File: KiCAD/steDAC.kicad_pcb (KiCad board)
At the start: 2 copper layers, 100 x 80 mm, 154 parts, among them IC10 ADP7182ACPZN-R7, IC11 ADP150AUJZ-3.3-R7, IC2 ES9038Q2M, IC3 ATSAMS70N20A-AN, IC4 ADP150AUJZ-3.3-R7, IC5 ADP150AUJZ-3.3-R7, IC6 ADP150AUJZ-3.3-R7, IC7 ADP150AUJZ-3.3-R7, IC8 LT1026CS8#PBF, IC9 ADP7118ARDZ, J2 USB4105-GF-A, J3 Conn_02x05_Odd_Even, J5 Conn_01x02, J6 Conn_01x04, J7 STX-3120-5B-284C, U2 OPA1612-Q1, U3 OPA1612-Q1, U4 OPA1622, Y2 SiT8209AI-21-33S-100.000000X, Y3 12MHz

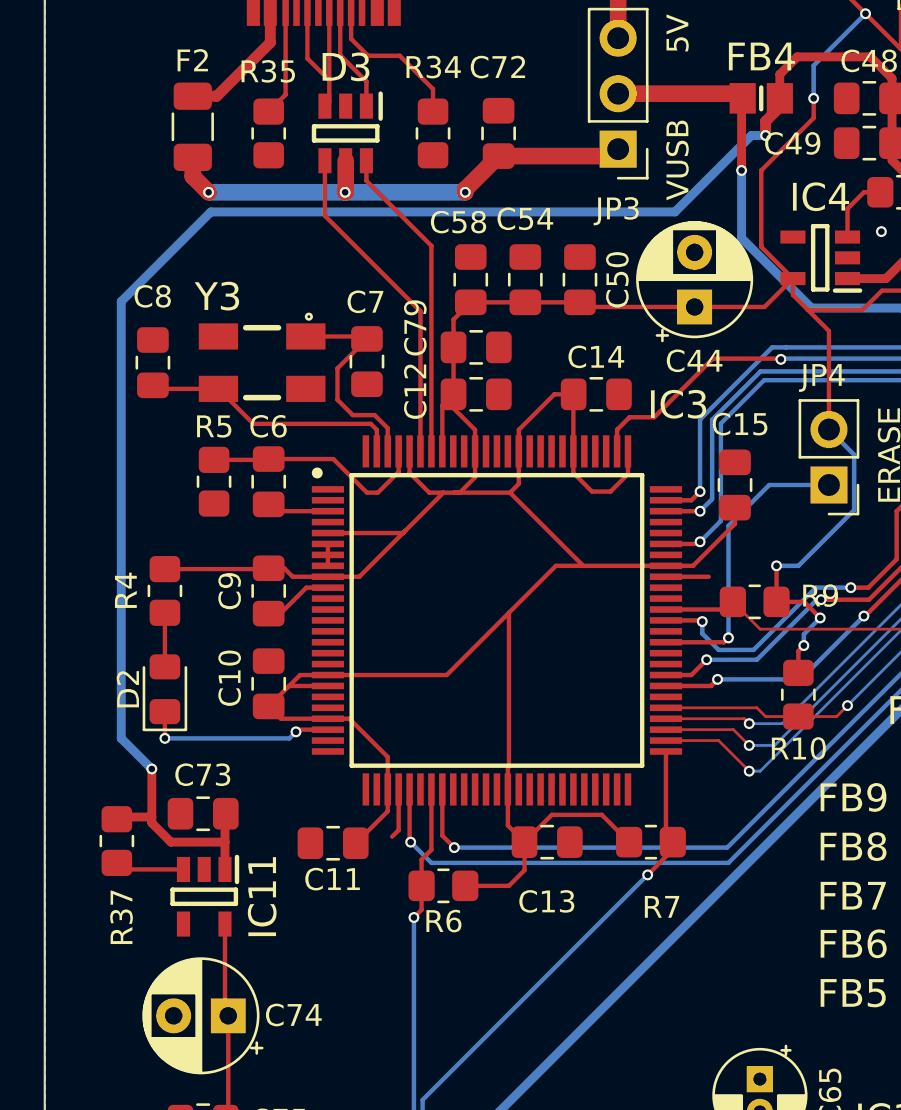
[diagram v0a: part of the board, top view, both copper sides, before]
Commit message: Updating BOM generator script
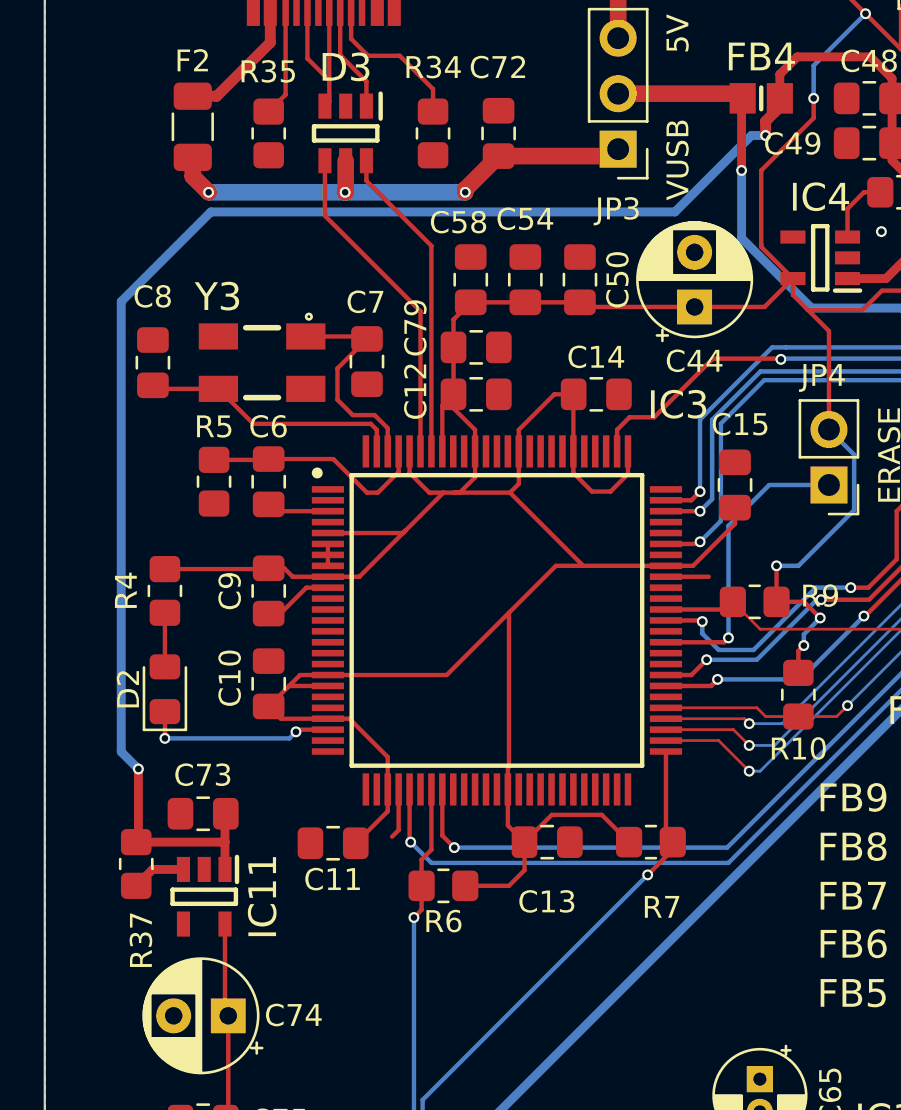
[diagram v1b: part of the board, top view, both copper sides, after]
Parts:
- moved R37 1.37 mm to (92.1, 100.9)
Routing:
- net Net-(IC11-Pad3): track 3.17 -> 2.47 mm
- net MCU_5V: track 86.2 -> 85.6 mm
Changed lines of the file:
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@@
       (sketchpadsonfab false)
       (subtractmaskfromsilk false)
-      (outputformat 4)
+      (outputformat 1)
       (mirror false)
       (drillshape 0)
@@
   )
   (footprint "Resistor_SMD:R_0805_2012Metric_Pad1.20x1.40mm_HandSolder" (layer "F.Cu")
-    (at 91.2125 99.85 90)
+    (at 92.1 100.9 90)
     (descr "Resistor SMD 0805 (2012 Metric), square (rectangular) end terminal, IPC_7351 nominal with elongated pad for handsoldering. (Body size source: IPC-SM-782 page 72, https://www.pcb-3d.com/wordpress/wp-content/uploads/ipc-sm-782a_amendment_1_and_2.pdf), generated with kicad-footprint-generator")
     (tags "resistor handsolder")
@@
   )
   (dimension (type aligned) (layer "Cmts.User")
+    (pts (xy 156.1625 131.65) (xy 187.9 131.65))
+    (height 12.749999)
+    (gr_text "31.7375 mm" (at 172.03125 143.249999) (layer "Cmts.User")
+      (effects (font (size 1 1) (thickness 0.15)))
+    )
+    (format (units 3) (units_format 1) (precision 4))
+    (style (thickness 0.15) (arrow_length 1.27) (text_position_mode 0) (extension_height 0.58642) (extension_offset 0.5) keep_text_aligned)
+  )
+  (dimension (type aligned) (layer "Cmts.User")
     (pts (xy 156.1625 131.65) (xy 156.1625 134.65))
     (height 15.75)
@@
     (style (thickness 0.15) (arrow_length 1.27) (text_position_mode 0) (extension_height 0.58642) (extension_offset 0.5) keep_text_aligned)
   )
+  (dimension (type aligned) (layer "Cmts.User")
+    (pts (xy 96.2175 60.415) (xy 87.9 60.415))
+    (height 11.605391)
+    (gr_text "8.3175 mm" (at 92.05875 47.659609) (layer "Cmts.User")
+      (effects (font (size 1 1) (thickness 0.15)))
+    )
+    (format (units 3) (units_format 1) (precision 4))
+    (style (thickness 0.15) (arrow_length 1.27) (text_position_mode 0) (extension_height 0.58642) (extension_offset 0.5) keep_text_aligned)
+  )
   (segment (start 160.7125 92.15) (end 160.7125 91.6375) (width 0.2) (layer "F.Cu") (net 1))
   (segment (start 160.7125 91.6375) (end 162.9125 89.4375) (width 0.2) (layer "F.Cu") (net 1))
@@
   (segment (start 170.375 128.65) (end 167.6125 128.65) (width 0.2032) (layer "F.Cu") (net 26))
   (segment (start 126.7 68.6875) (end 128.1625 70.15) (width 0.4064) (layer "F.Cu") (net 27))
-  (segment (start 92.8125 98.75) (end 91.3125 98.75) (width 0.4064) (layer "F.Cu") (net 27))
   (segment (start 96.2 98.6) (end 96.1625 98.6375) (width 0.2032) (layer "F.Cu") (net 27))
-  (segment (start 92.8125 99.023085) (end 93.689415 99.9) (width 0.4064) (layer "F.Cu") (net 27))
   (segment (start 121.5625 66.25) (end 120.9125 66.9) (width 0.5) (layer "F.Cu") (net 27))
-  (segment (start 93.689415 99.9) (end 96.1625 99.9) (width 0.4064) (layer "F.Cu") (net 27))
   (segment (start 122.3625 63.95) (end 125.7125 63.95) (width 0.4064) (layer "F.Cu") (net 27))
   (segment (start 121.5625 64.75) (end 122.3625 63.95) (width 0.4064) (layer "F.Cu") (net 27))
-  (segment (start 91.3125 98.75) (end 91.2125 98.85) (width 0.4064) (layer "F.Cu") (net 27))
   (segment (start 126.425 74.1) (end 124.6625 74.1) (width 0.4064) (layer "F.Cu") (net 27))
-  (segment (start 92.8125 98.75) (end 92.8125 99.023085) (width 0.4064) (layer "F.Cu") (net 27))
+  (segment (start 96.1625 99.9) (end 92.1 99.9) (width 0.4064) (layer "F.Cu") (net 27))
   (segment (start 127.775 72.75) (end 126.425 74.1) (width 0.4064) (layer "F.Cu") (net 27))
   (segment (start 126.7 64.9375) (end 126.7 65.85) (width 0.4064) (layer "F.Cu") (net 27))
   (segment (start 126.7 67.9) (end 126.7 68.6875) (width 0.4064) (layer "F.Cu") (net 27))
   (segment (start 125.7125 63.95) (end 126.7 64.9375) (width 0.4064) (layer "F.Cu") (net 27))
-  (segment (start 92.8125 96.55) (end 92.8125 98.75) (width 0.4064) (layer "F.Cu") (net 27))
   (segment (start 121.5625 65.85) (end 121.5625 64.75) (width 0.4064) (layer "F.Cu") (net 27))
   (segment (start 128.1625 70.15) (end 128.1625 72.3625) (width 0.4064) (layer "F.Cu") (net 27))
   (segment (start 120.9125 66.9) (end 120.9125 67.55) (width 0.5) (layer "F.Cu") (net 27))
+  (segment (start 92.1 99.9) (end 92.2 99.8) (width 0.4064) (layer "F.Cu") (net 27))
   (segment (start 126.7 65.85) (end 126.7 67.9) (width 0.4064) (layer "F.Cu") (net 27))
   (segment (start 128.1625 72.3625) (end 127.775 72.75) (width 0.4064) (layer "F.Cu") (net 27))
   (segment (start 96.1625 98.6375) (end 96.1625 99.9) (width 0.4064) (layer "F.Cu") (net 27))
   (segment (start 121.5625 65.85) (end 121.5625 66.25) (width 0.2032) (layer "F.Cu") (net 27))
+  (segment (start 92.2 99.8) (end 92.2 96.55) (width 0.4064) (layer "F.Cu") (net 27))
   (segment (start 96.1625 99.9) (end 96.1625 101.15) (width 0.4064) (layer "F.Cu") (net 27))
-  (via (at 92.8125 96.55) (size 0.5) (drill 0.3) (layers "F.Cu" "B.Cu") (net 27))
+  (via (at 92.2 96.55) (size 0.5) (drill 0.3) (layers "F.Cu" "B.Cu") (net 27))
   (via (at 120.9125 67.55) (size 0.5) (drill 0.3) (layers "F.Cu" "B.Cu") (net 27))
-  (segment (start 120.2625 67.55) (end 116.7625 71.05) (width 0.4064) (layer "B.Cu") (net 27))
-  (segment (start 91.4125 95.15) (end 92.8125 96.55) (width 0.4064) (layer "B.Cu") (net 27))
-  (segment (start 116.7625 71.05) (end 95.5125 71.05) (width 0.4064) (layer "B.Cu") (net 27))
-  (segment (start 95.5125 71.05) (end 91.4125 75.15) (width 0.4064) (layer "B.Cu") (net 27))
-  (segment (start 120.9125 67.55) (end 120.2625 67.55) (width 0.4064) (layer "B.Cu") (net 27))
-  (segment (start 91.4125 75.15) (end 91.4125 95.15) (width 0.4064) (layer "B.Cu") (net 27))
+  (segment (start 95.5125 71.05) (end 116.7625 71.05) (width 0.4064) (layer "B.Cu") (net 27))
+  (segment (start 120.2625 67.55) (end 120.9125 67.55) (width 0.4064) (layer "B.Cu") (net 27))
+  (segment (start 116.7625 71.05) (end 120.2625 67.55) (width 0.4064) (layer "B.Cu") (net 27))
+  (segment (start 91.4125 75.15) (end 95.5125 71.05) (width 0.4064) (layer "B.Cu") (net 27))
+  (segment (start 92.2 96.55) (end 91.4125 95.7625) (width 0.4064) (layer "B.Cu") (net 27))
+  (segment (start 91.4125 95.7625) (end 91.4125 75.15) (width 0.4064) (layer "B.Cu") (net 27))
   (segment (start 141.875 85.65) (end 141.875 86.575) (width 0.4064) (layer "F.Cu") (net 28))
   (segment (start 114.9505 116.765) (end 112.5525 116.765) (width 0.4064) (layer "F.Cu") (net 28))
@@
   (segment (start 124.6625 70.9) (end 124.6625 72.2) (width 0.2032) (layer "F.Cu") (net 124))
   (segment (start 125.4125 70.15) (end 126.1625 70.15) (width 0.2032) (layer "F.Cu") (net 124))
-  (segment (start 91.2125 100.85) (end 91.5125 101.15) (width 0.2) (layer "F.Cu") (net 131))
-  (segment (start 91.5125 101.15) (end 94.2625 101.15) (width 0.2) (layer "F.Cu") (net 131))
+  (segment (start 92.85 101.15) (end 92.1 101.9) (width 0.4064) (layer "F.Cu") (net 131))
+  (segment (start 94.2625 101.15) (end 92.85 101.15) (width 0.4064) (layer "F.Cu") (net 131))
   (segment (start 105.6875 65.425) (end 105.6875 66.455) (width 0.2032) (layer "F.Cu") (net 134))
   (segment (start 104.1625 63.9) (end 105.6875 65.425) (width 0.2032) (layer "F.Cu") (net 134))

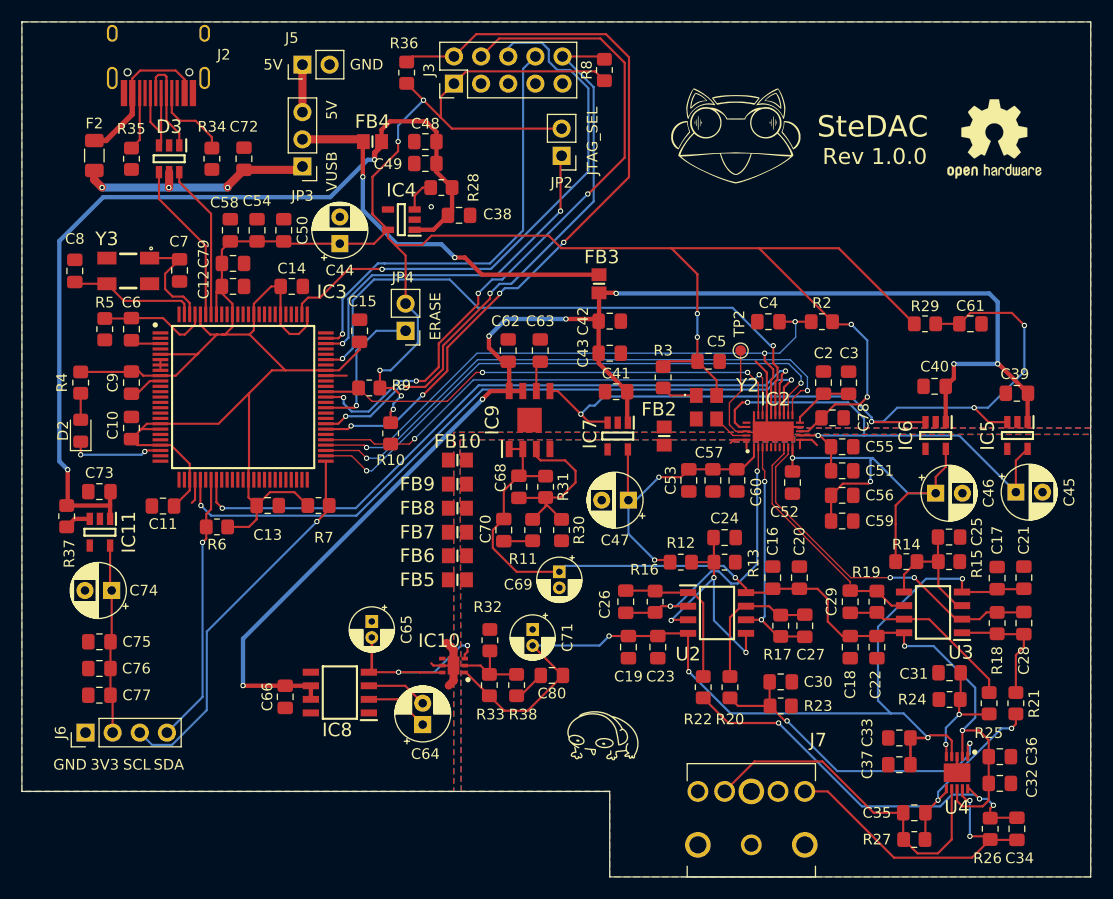
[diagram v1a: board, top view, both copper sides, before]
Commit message: [REV1.0.1] Rerouting some traces in the output stage. Adding rev1.0.1 gerbers
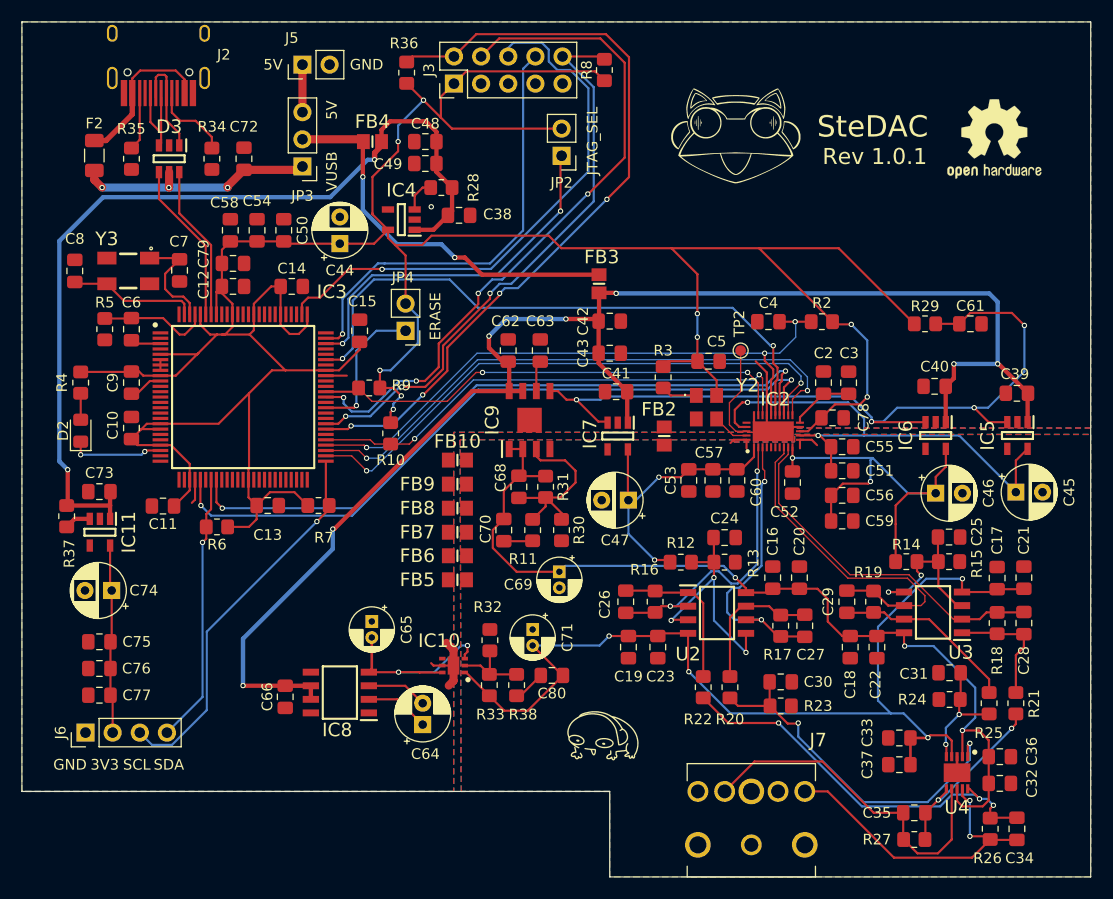
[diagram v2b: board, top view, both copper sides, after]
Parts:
- moved C29 0.31 mm to (165.1, 108.9)
- moved R19 0.31 mm to (167.6, 108.9)
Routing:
- net DAC_OUTL_P: track 22.5 -> 31.8 mm
- net DAC_OUTR_P: track 22.5 -> 27.0 mm
- net Net-(C30-Pad1): track 30.5 -> 34.1 mm
- net /Output Stage/VBias_L: track 13.0 -> 16.3 mm, vias 0 -> 2
- net DAC_5V: track 138.3 -> 139.4 mm
- net DAC_OUTL_N: track 33.7 -> 33.3 mm, vias 2 -> 0
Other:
- board text added: "Rev 1.0.1"
- board text removed: "Rev 1.0.0"

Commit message: Fixing 3.3V being fed to VDDCORE. Swaping 3.3V LDOs to onsemi ones with higher output current
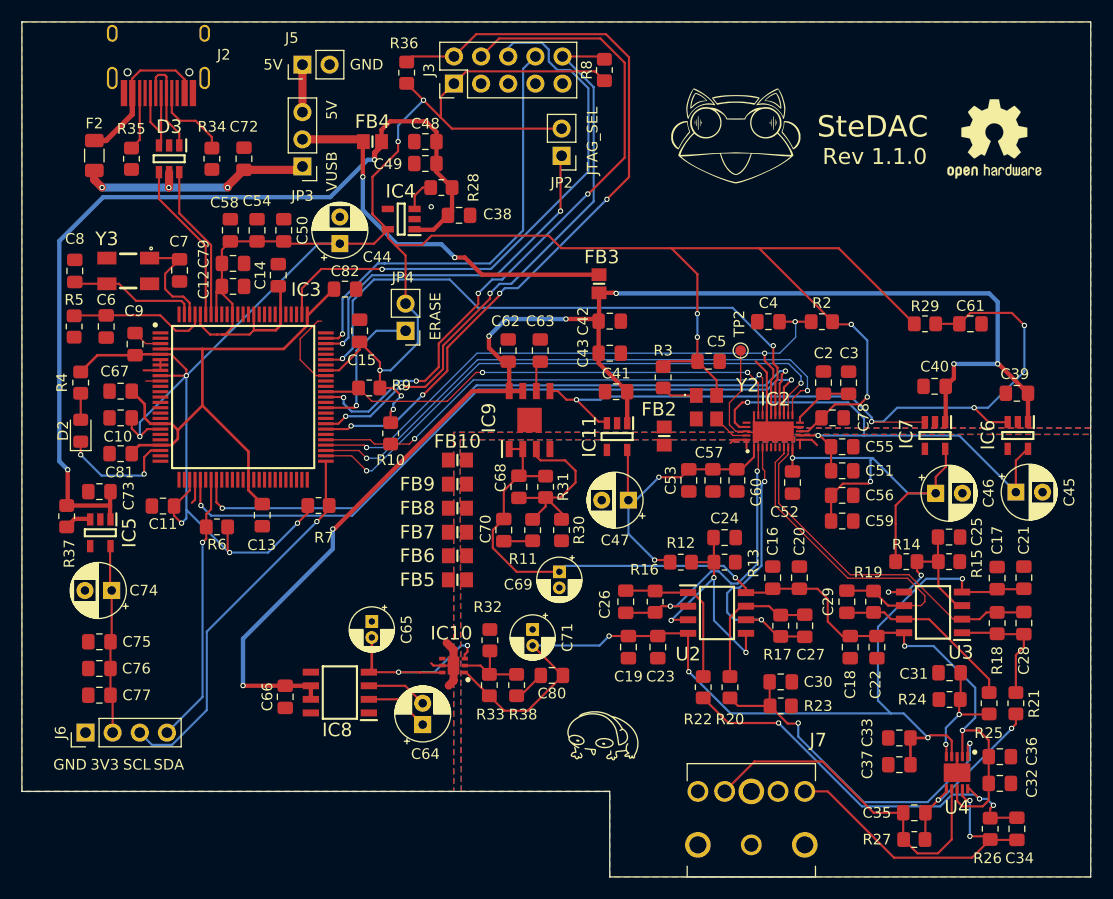
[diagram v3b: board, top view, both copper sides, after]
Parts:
- added C67: 0.1u, Capacitor_SMD:C_0805_2012Metric_Pad1.18x1.45mm_HandSolder, F.Cu at (97.2, 89.2)
- added C81: 0.1u, Capacitor_SMD:C_0805_2012Metric_Pad1.18x1.45mm_HandSolder, F.Cu at (97.2, 95.0)
- added C82: 0.1u, Capacitor_SMD:C_0805_2012Metric_Pad1.18x1.45mm_HandSolder, F.Cu at (118.2, 79.7)
- IC11, IC4, IC5, IC6, IC7: value ADP150AUJZ-3.3-R7 -> NCP161ASN330T1G; footprint SamacSys_Parts:SOT95P280X100-5N -> SamacSys_Parts:SOT95P280X145-5N
- U2, U3: value OPA1612-Q1 -> OPA1612
- moved IC5 86.3 mm to (95.2, 102.5)
- moved IC11 49.2 mm to (143.6, 93.5)
- moved IC7 29.7 mm to (173.3, 93.3)
- moved IC6 7.69 mm to (181.1, 93.3)
- moved C9 3.62 mm to (98.5, 84.8), turned to 90 degrees
- moved R5 2.87 mm to (92.8, 83.2)
- moved C6 2.38 mm to (95.8, 83.2)
- moved C14 1.64 mm to (111.9, 78.3), turned to 90 degrees
- moved C10 1.39 mm to (97.2, 91.7), turned to 180 degrees
- moved C13 1.04 mm to (110.4, 100.8), turned to -90 degrees
- moved IC4 0.05 mm to (123.4, 73.1)
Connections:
- C13 pad 1: +3V3 -> +1V2
- IC11 pad 1: MCU_5V -> DAC_5V
- IC11 pad 3: Net-(IC11-Pad3) -> DAC_PWR_EN
- IC11 pad 5: OLED_3V3 -> AVCC_R
- IC3 pad 18: +3V3 -> +1V2
- IC3 pad 22: +3V3 -> +1V2
- IC3 pad 39: +3V3 -> +1V2
- IC3 pad 4: unconnected-(IC3-Pad4) -> +1V2
- IC3 pad 76: +3V3 -> +1V2
- IC5 pad 1: DAC_5V -> MCU_5V
- IC5 pad 3: DAC_PWR_EN -> Net-(IC5-Pad3)
- IC5 pad 5: +3.3VDAC -> OLED_3V3
- IC6 pad 5: AVCC_L -> +3.3VDAC
- IC7 pad 5: AVCC_R -> AVCC_L
- R37 pad 1: Net-(IC11-Pad3) -> Net-(IC5-Pad3)
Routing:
- net +1V2: track 0.00 -> 51.6 mm
- net GND: track 30.7 -> 36.0 mm
- net Net-(C6-Pad1): track 10.4 -> 13.1 mm
- net +3V3: track 301.0 -> 303.6 mm, vias 9 -> 14
- net Net-(D2-Pad1): track 8.85 -> 11.4 mm
- net Net-(IC5-Pad3): track 0.00 -> 2.47 mm
- net Net-(IC11-Pad3): track 2.47 -> 0.00 mm
- net JTAG_TDO: track 51.6 -> 52.5 mm
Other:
- board text added: "Rev 1.1.0"
- board text removed: "Rev 1.0.1"
